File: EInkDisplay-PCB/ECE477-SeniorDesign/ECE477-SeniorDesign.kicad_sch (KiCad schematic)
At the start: 0 parts

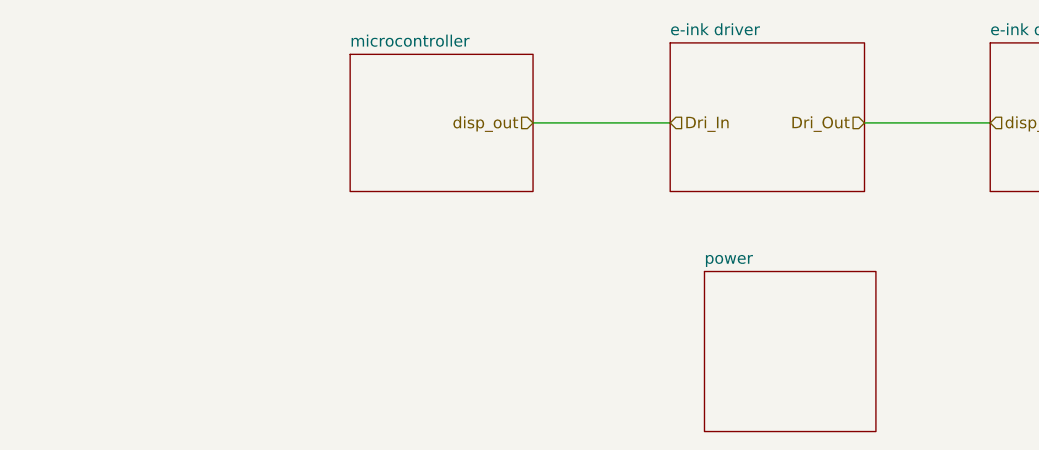
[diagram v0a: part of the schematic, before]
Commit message: Add Blocks
Adding USB-UART block
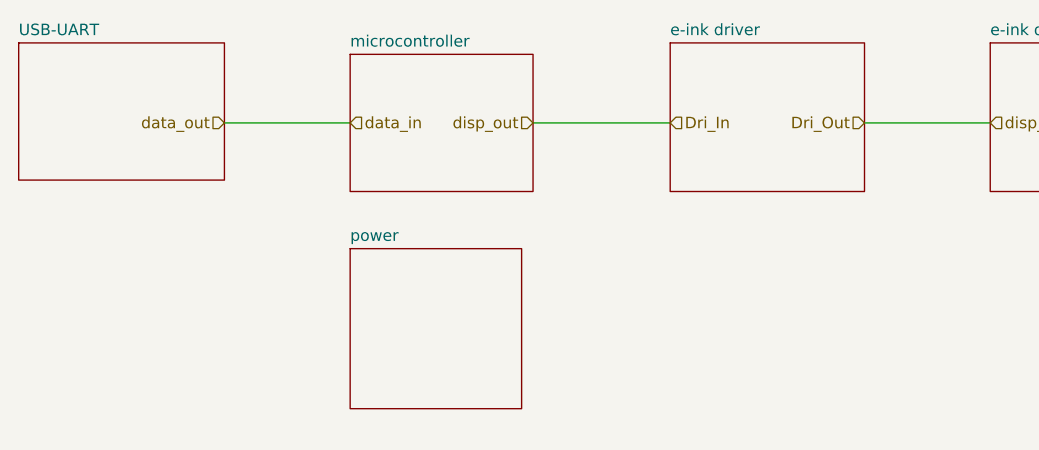
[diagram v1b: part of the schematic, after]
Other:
- added sheet USB-UART (untitled.kicad_sch)
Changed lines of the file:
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@@
+		)
+	)
+	(wire
+		(pts
+			(xy 57.15 55.88) (xy 71.12 55.88)
+		)
+		(stroke
+			(width 0)
+			(type default)
 		)
 	)
@@
 			)
 			(justify left)
+		)
+	)
+	(hierarchical_label "data_in"
+		(shape input)
+		(at 71.12 55.88 0)
+		(effects
+			(font
+				(size 1.27 1.27)
+			)
+			(justify left)
+		)
+	)
+	(hierarchical_label "data_out"
+		(shape input)
+		(at 57.15 55.88 180)
+		(effects
+			(font
+				(size 1.27 1.27)
+			)
+			(justify right)
 		)
 	)
@@
 	)
 	(sheet
-		(at 110.49 72.39)
+		(at 34.29 46.99)
+		(size 22.86 15.24)
+		(fields_autoplaced yes)
+		(stroke
+			(width 0.1524)
+			(type solid)
+		)
+		(fill
+			(color 0 0 0 0.0000)
+		)
+		(property "Sheetname" "USB-UART"
+			(at 34.29 46.2784 0)
+			(effects
+				(font
+					(size 1.27 1.27)
+				)
+				(justify left bottom)
+			)
+		)
+		(property "Sheetfile" "untitled.kicad_sch"
+			(at 34.29 62.8146 0)
+			(effects
+				(font
+					(size 1.27 1.27)
+				)
+				(justify left top)
+				(hide yes)
+			)
+		)
+		(instances
+			(project "ECE477-SeniorDesign"
+				(path "/527ae649-08be-4368-9cf9-441ebba18eca"
+					(page "6")
+				)
+			)
+		)
+	)
+	(sheet
+		(at 71.12 69.85)
 		(size 19.05 17.78)
 		(fields_autoplaced yes)
@@
 		)
 		(property "Sheetname" "power"
-			(at 110.49 71.6784 0)
-			(effects
-				(font
-					(size 1.27 1.27)
-				)
-				(justify left bottom)
-			)
-		)
-		(property "Sheetfile" "untitled.kicad_sch"
-			(at 110.49 90.7546 0)
-			(effects
-				(font
+			(at 71.12 69.1384 0)
+			(effects
+				(font
+					(size 1.27 1.27)
+				)
+				(justify left bottom)
+			)
+		)
+		(property "Sheetfile" "untitled.kicad_sch"
+			(at 71.12 88.2146 0)
+			(effects
+				(font

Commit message: Update
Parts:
- added C1, C2: C, symbol Device:C
- added D1, D2, D3: MBR0530, Diode_SMD:D_SOD-123, symbol Diode:MBR0530
- added L1: L, symbol Device:L
- added Q1: BSS138, Package_TO_SOT_SMD:SOT-23, symbol Transistor_FET:BSS138
- added R1, R2: R, symbol Device:R
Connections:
- new net: C1.1, D3.1 (K), L1.2, Q1.3 (D)
- new net: C1.2, D1.2 (A), D2.1 (K)
- new net: Q1.1 (G), R1.1
- new net: Q1.2 (S), R2.1
- new net +3.3V: C2.1, L1.1
- new net GND: C2.2, D1.1 (K), R1.2, R2.2
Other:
- removed sheet USB-UART
- removed sheet e-ink display
- removed sheet e-ink driver
- removed sheet microcontroller
- removed sheet power
- added sheet Power (untitled.kicad_sch)

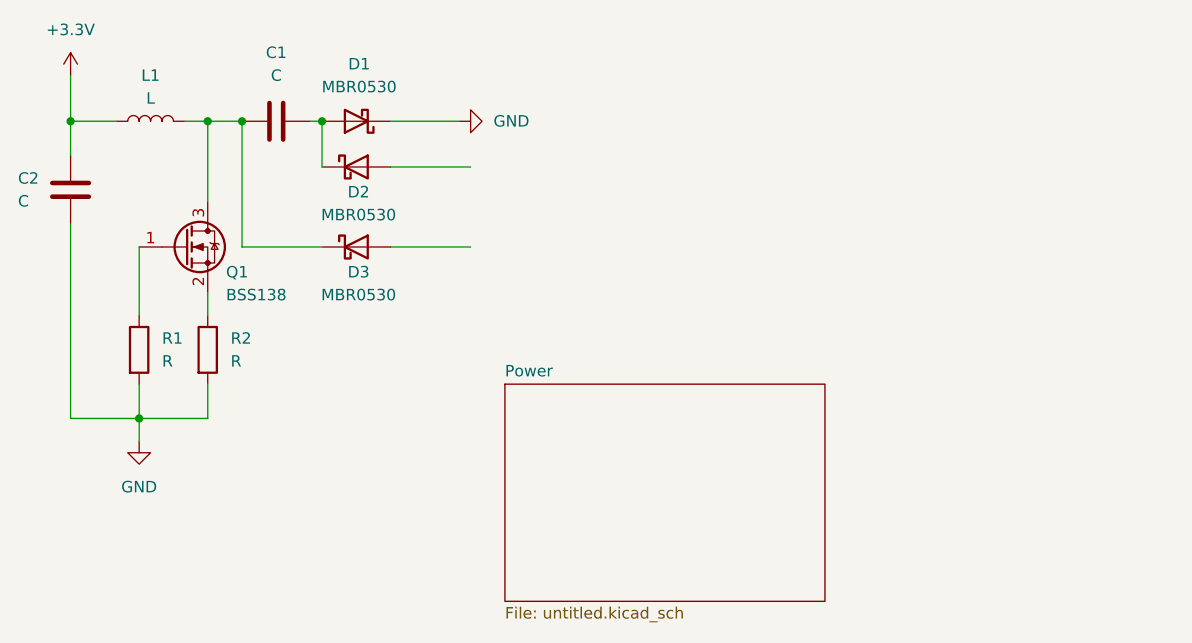
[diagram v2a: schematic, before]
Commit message: Adding Component Library
-named einkcomponent library
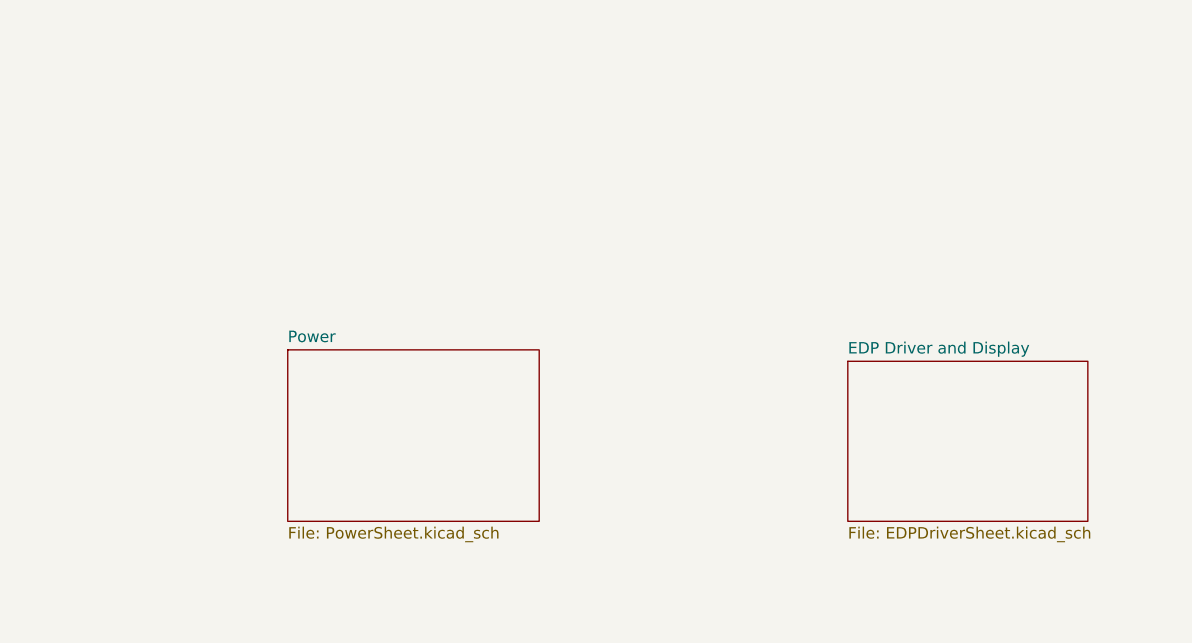
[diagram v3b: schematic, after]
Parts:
- removed C1, C2: C, symbol Device:C
- removed D1, D2, D3: MBR0530, Diode_SMD:D_SOD-123, symbol Diode:MBR0530
- removed L1: L, symbol Device:L
- removed Q1: BSS138, Package_TO_SOT_SMD:SOT-23, symbol Transistor_FET:BSS138
- removed R1, R2: R, symbol Device:R
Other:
- added sheet EDP Driver and Display (EDPDriverSheet.kicad_sch)
- sheet Power: file untitled.kicad_sch -> PowerSheet.kicad_sch

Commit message: USB Complete
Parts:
- added C1, C4: 0.1uF, symbol Device:C_Small
- added C2: 1uF, symbol Device:C_Small
- added C3: 4.7uF, symbol Device:C_Small
- added EinkDispCon: ~, symbol EinkComponentLibrary:EinkDisplay
- added J1: USB_B, symbol Connector:USB_B
- added U1: STM32L496ZGTxP, Package_QFP:LQFP-144_20x20mm_P0.5mm, symbol MCU_ST_STM32L4:STM32L496ZGTxP
- added U2: CP2102-GMR, INTERFACE-CP2102-GMR_QFN28_:QFN28G_0.5-5X5MM, symbol EinkComponentLibrary:INTERFACE-CP2102-GMR_QFN28_
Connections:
- new net: C3.2, C4.2, U2.6 (VDD)
- new net: J1.3 (D+), U2.4 (D+)
- new net: J1.2 (D-), U2.5 (D-)
- new net: U1.107 (VSS), U1.120 (VSS), U1.130 (VSS), U1.143 (VSS), U1.16 (VSS), U1.38 (VSS), U1.51 (VSS), U1.61 (VSS), U1.71 (VSS), U1.83 (VSS), U1.94 (VSS)
- new net GND: C1.2, C2.2, C3.1, C4.1, J1.4 (GND), U2.29 (GND@1), U2.3 (GND)
- new net USART_RX: U2.26 (TXD)
- new net USART_TX: U2.25 (RXD)
- new net VBUS: C1.1, C2.1, J1.1 (VBUS), U2.7 (REGIN), U2.8 (VBUS)
- no-connect marks 0 -> 21
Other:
- removed sheet EDP Driver and Display
- removed sheet Power

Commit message: Lot of changes
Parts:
- removed C1, C4: 0.1uF, symbol Device:C_Small
- removed C2: 1uF, symbol Device:C_Small
- removed C3: 4.7uF, symbol Device:C_Small
- removed J1: USB_B, symbol Connector:USB_B
- removed U1: STM32L496ZGTxP, Package_QFP:LQFP-144_20x20mm_P0.5mm, symbol MCU_ST_STM32L4:STM32L496ZGTxP
- removed U2: CP2102-GMR, INTERFACE-CP2102-GMR_QFN28_:QFN28G_0.5-5X5MM, symbol EinkComponentLibrary:INTERFACE-CP2102-GMR_QFN28_
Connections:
- no-connect marks 21 -> 0
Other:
- added sheet ExtraPeriphs (untitled.kicad_sch)
- added sheet LipoPower (LiPoPower_Module_Sheet.kicad_sch)
- added sheet MCU (MCU_Module_Sheet.kicad_sch)
- added sheet USB-UART (USB-UART_Module_Sheet.kicad_sch)

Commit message: push
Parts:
- removed EinkDispCon: ~, symbol EinkComponentLibrary:EinkDisplay
- added EinkDispCon2: ~, symbol EinkComponentLibrary:EinkDisplay
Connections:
- new net +3.3V: EinkDispCon2.1 (VCC)
- new net GND: EinkDispCon2.2 (GND)
- new net MCU/SPI1_MOSI: EinkDispCon2.3 (DIN)
- new net MCU/SPI1_SCK: EinkDispCon2.4 (CLK)
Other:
- sheet MCU ports: added SPI1_MOSI, SPI1_SCK, USART1_RX, USART1_TX; removed none
- sheet USB-UART ports: added USART1_RX, USART1_TX; removed none

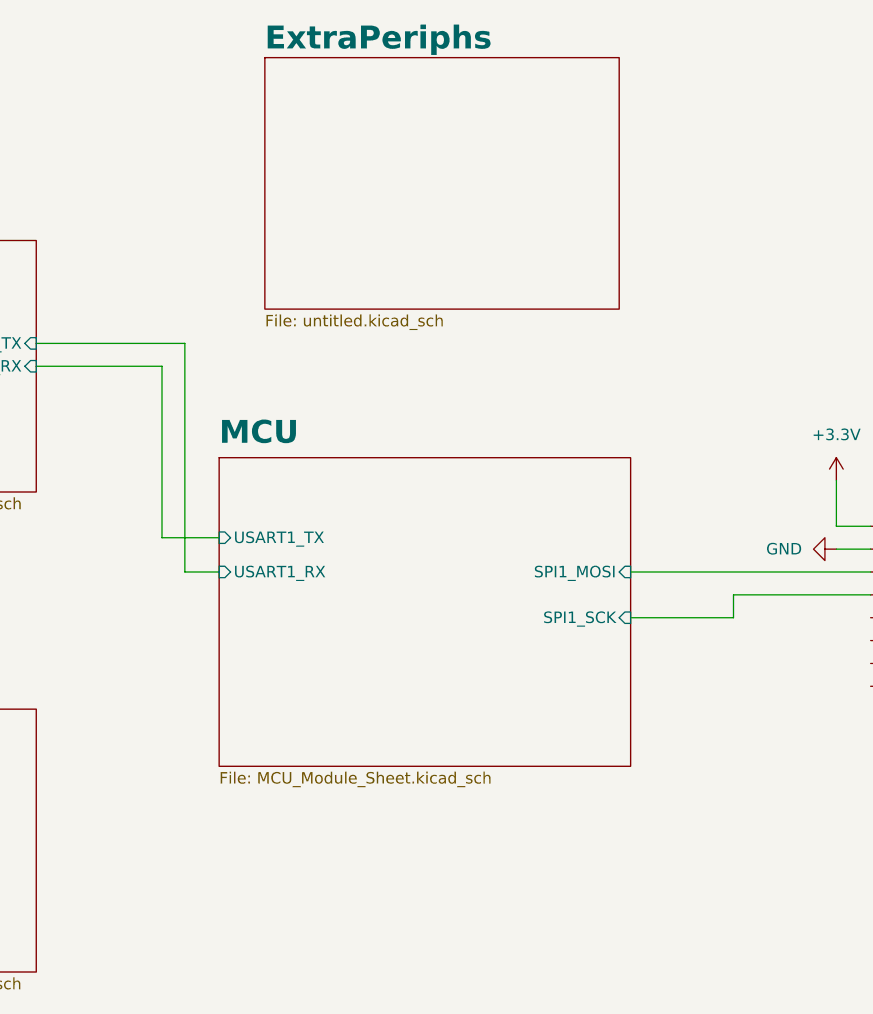
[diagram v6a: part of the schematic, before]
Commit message: Adding SD
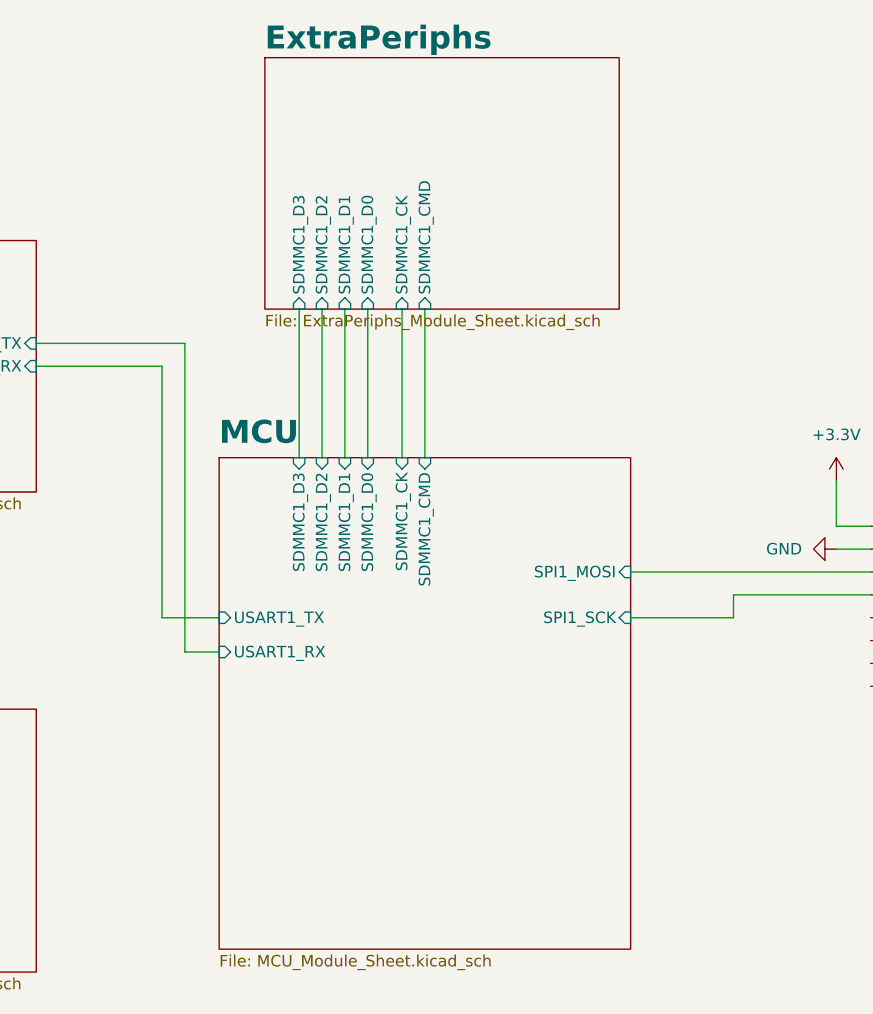
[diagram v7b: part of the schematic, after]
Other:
- sheet ExtraPeriphs: file untitled.kicad_sch -> ExtraPeriphs_Module_Sheet.kicad_sch
- sheet ExtraPeriphs ports: added SDMMC1_CK, SDMMC1_CMD, SDMMC1_D0, SDMMC1_D1, SDMMC1_D2, SDMMC1_D3; removed none
- sheet MCU ports: added SDMMC1_CK, SDMMC1_CMD, SDMMC1_D0, SDMMC1_D1, SDMMC1_D2, SDMMC1_D3; removed none
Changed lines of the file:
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@@
 	(wire
 		(pts
-			(xy 110.49 95.25) (xy 116.84 95.25)
+			(xy 110.49 104.14) (xy 116.84 104.14)
+		)
+		(stroke
+			(width 0)
+			(type default)
+		)
+	)
+	(wire
+		(pts
+			(xy 137.16 69.85) (xy 137.16 86.36)
 		)
 		(stroke
@@
 	(wire
 		(pts
-			(xy 110.49 76.2) (xy 110.49 95.25)
+			(xy 133.35 69.85) (xy 133.35 86.36)
+		)
+		(stroke
+			(width 0)
+			(type default)
+		)
+	)
+	(wire
+		(pts
+			(xy 110.49 76.2) (xy 110.49 104.14)
 		)
 		(stroke
@@
 	(wire
 		(pts
+			(xy 139.7 69.85) (xy 139.7 86.36)
+		)
+		(stroke
+			(width 0)
+			(type default)
+		)
+	)
+	(wire
+		(pts
 			(xy 189.23 93.98) (xy 185.42 93.98)
 		)
@@
 	(wire
 		(pts
-			(xy 113.03 99.06) (xy 116.84 99.06)
+			(xy 113.03 107.95) (xy 116.84 107.95)
 		)
 		(stroke
@@
 	(wire
 		(pts
-			(xy 113.03 73.66) (xy 113.03 99.06)
+			(xy 113.03 73.66) (xy 113.03 107.95)
 		)
 		(stroke
@@
 		(pts
 			(xy 173.99 101.6) (xy 189.23 101.6)
+		)
+		(stroke
+			(width 0)
+			(type default)
+		)
+	)
+	(wire
+		(pts
+			(xy 128.27 69.85) (xy 128.27 86.36)
+		)
+		(stroke
+			(width 0)
+			(type default)
+		)
+	)
+	(wire
+		(pts
+			(xy 130.81 69.85) (xy 130.81 86.36)
+		)
+		(stroke
+			(width 0)
+			(type default)
+		)
+	)
+	(wire
+		(pts
+			(xy 125.73 69.85) (xy 125.73 86.36)
 		)
 		(stroke
@@
 			)
 		)
-		(property "Sheetfile" "untitled.kicad_sch"
+		(property "Sheetfile" "ExtraPeriphs_Module_Sheet.kicad_sch"
 			(at 121.92 70.4346 0)
 			(effects
@@
 				)
 				(justify left top)
+			)
+		)
+		(pin "SDMMC1_D2" input
+			(at 128.27 69.85 270)
+			(effects
+				(font
+					(size 1.27 1.27)
+				)
+				(justify left)
+			)
+		)
+		(pin "SDMMC1_D3" input
+			(at 125.73 69.85 270)
+			(effects
+				(font
+					(size 1.27 1.27)
+				)
+				(justify left)
+			)
+		)
+		(pin "SDMMC1_D1" input
+			(at 130.81 69.85 270)
+			(effects
+				(font
+					(size 1.27 1.27)
+				)
+				(justify left)
+			)
+		)
+		(pin "SDMMC1_D0" input
+			(at 133.35 69.85 270)
+			(effects
+				(font
+					(size 1.27 1.27)
+				)
+				(justify left)
+			)
+		)
+		(pin "SDMMC1_CK" input
+			(at 137.16 69.85 270)
+			(effects
+				(font
+					(size 1.27 1.27)
+				)
+				(justify left)
+			)
+		)
+		(pin "SDMMC1_CMD" input
+			(at 139.7 69.85 270)
+			(effects
+				(font
+					(size 1.27 1.27)
+				)
+				(justify left)
 			)
 		)
@@
 	(sheet
 		(at 116.84 86.36)
-		(size 45.72 34.29)
+		(size 45.72 54.61)
 		(fields_autoplaced yes)
 		(stroke
@@
 		)
 		(property "Sheetfile" "MCU_Module_Sheet.kicad_sch"
-			(at 116.84 121.2346 0)
+			(at 116.84 141.5546 0)
 			(effects
 				(font
@@
 		)
 		(pin "USART1_TX" input
-			(at 116.84 95.25 180)
+			(at 116.84 104.14 180)
 			(effects
 				(font
@@
 		)
 		(pin "USART1_RX" input
-			(at 116.84 99.06 180)
+			(at 116.84 107.95 180)
 			(effects
 				(font
@@
 			(effects
 				(font
+					(size 1.27 1.27)
+				)
+				(justify right)
+			)
+		)
+		(pin "SDMMC1_CK" input
+			(at 137.16 86.36 90)
+			(effects
+				(font
+					(size 1.27 1.27)
+				)
+				(justify right)
+			)
+		)
+		(pin "SDMMC1_CMD" input
+			(at 139.7 86.36 90)
+			(effects
+				(font
+					(size 1.27 1.27)
+				)
+				(justify right)
+			)
+		)
+		(pin "SDMMC1_D0" input
+			(at 133.35 86.36 90)
+			(effects
+				(font
+					(size 1.27 1.27)
+				)
+				(justify right)
+			)
+		)
+		(pin "SDMMC1_D1" input
+			(at 130.81 86.36 90)
+			(effects
+				(font
+					(size 1.27 1.27)
+				)
+				(justify right)
+			)
+		)
+		(pin "SDMMC1_D2" input
+			(at 128.27 86.36 90)
+			(effects
+				(font
+					(size 1.27 1.27)
+				)
+				(justify right)
+			)
+		)
+		(pin "SDMMC1_D3" input
+			(at 125.73 86.36 90)
+			(effects
+				(font

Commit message: fixing
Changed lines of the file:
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@@
-	(wire
-		(pts
-			(xy 137.16 69.85) (xy 137.16 86.36)
-		)
-		(stroke
-			(width 0)
-			(type default)
-		)
-	)
 	(wire
 		(pts
 			(xy 96.52 76.2) (xy 110.49 76.2)
-		)
-		(stroke
-			(width 0)
-			(type default)
-		)
-	)
-	(wire
-		(pts
-			(xy 133.35 69.85) (xy 133.35 86.36)
 		)
 		(stroke
@@
 		(pts
 			(xy 162.56 99.06) (xy 189.23 99.06)
-		)
-		(stroke
-			(width 0)
-			(type default)
-		)
-	)
-	(wire
-		(pts
-			(xy 139.7 69.85) (xy 139.7 86.36)
 		)
 		(stroke
@@
 		)
 		(stroke
-			(width 0)
-			(type default)
-		)
-	)
-	(wire
-		(pts
-			(xy 128.27 69.85) (xy 128.27 86.36)
-		)
-		(stroke
-			(width 0)
-			(type default)
-		)
-	)
-	(wire
-		(pts
-			(xy 130.81 69.85) (xy 130.81 86.36)
-		)
-		(stroke
